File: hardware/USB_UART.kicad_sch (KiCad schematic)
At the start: 15 parts, among them Q17 BC847BS-7-F, SW1 SW_SPDT, U14 CP2102N-QFN20

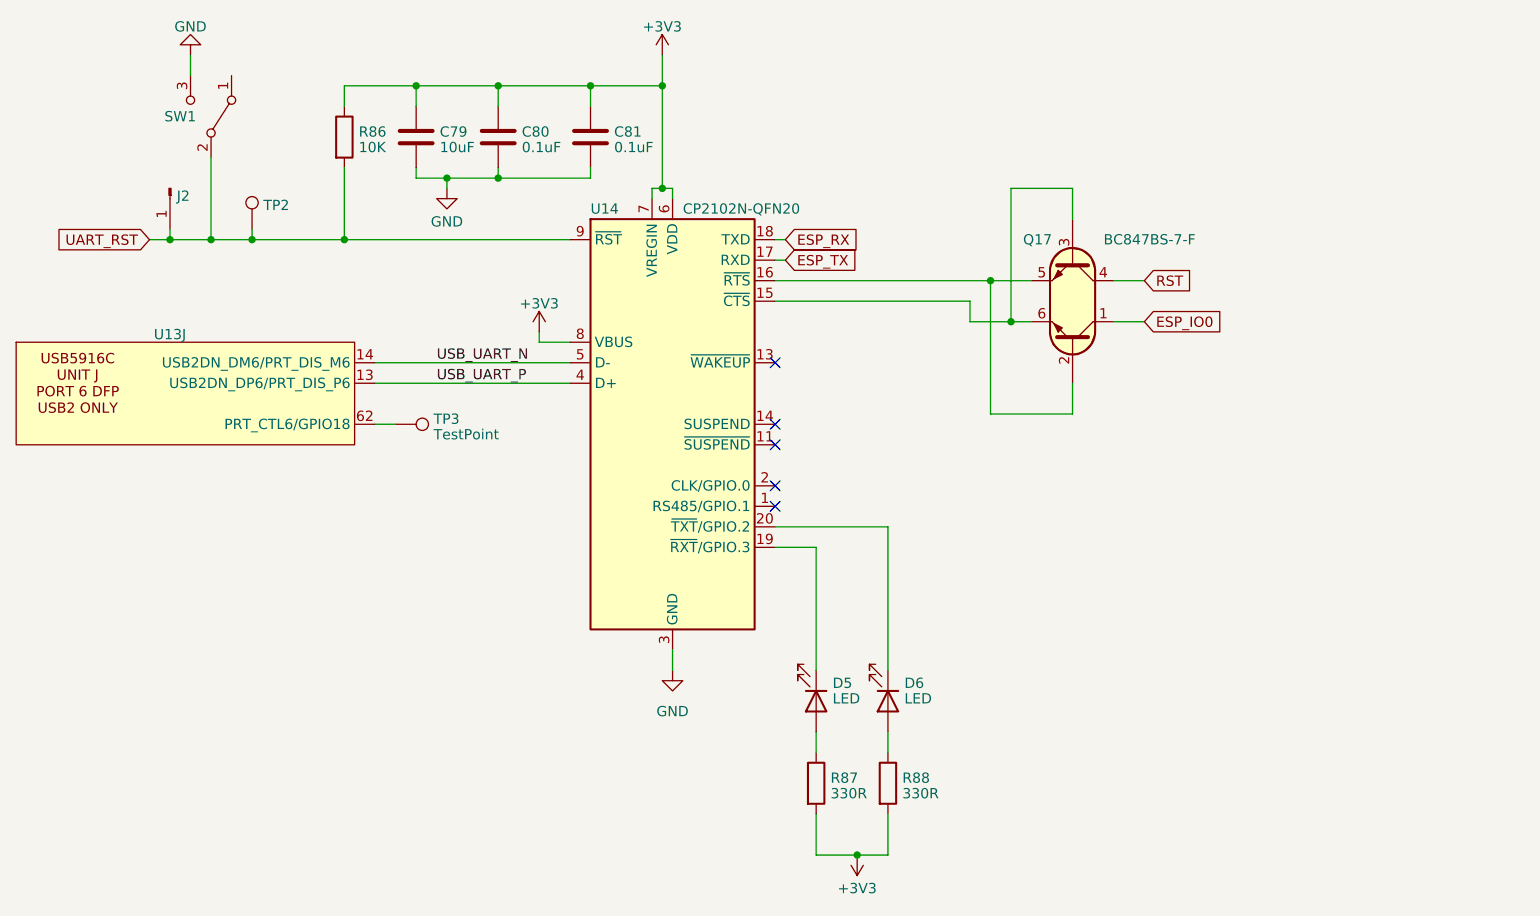
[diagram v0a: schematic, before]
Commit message: fixed DP issues and finneshed overall routeing
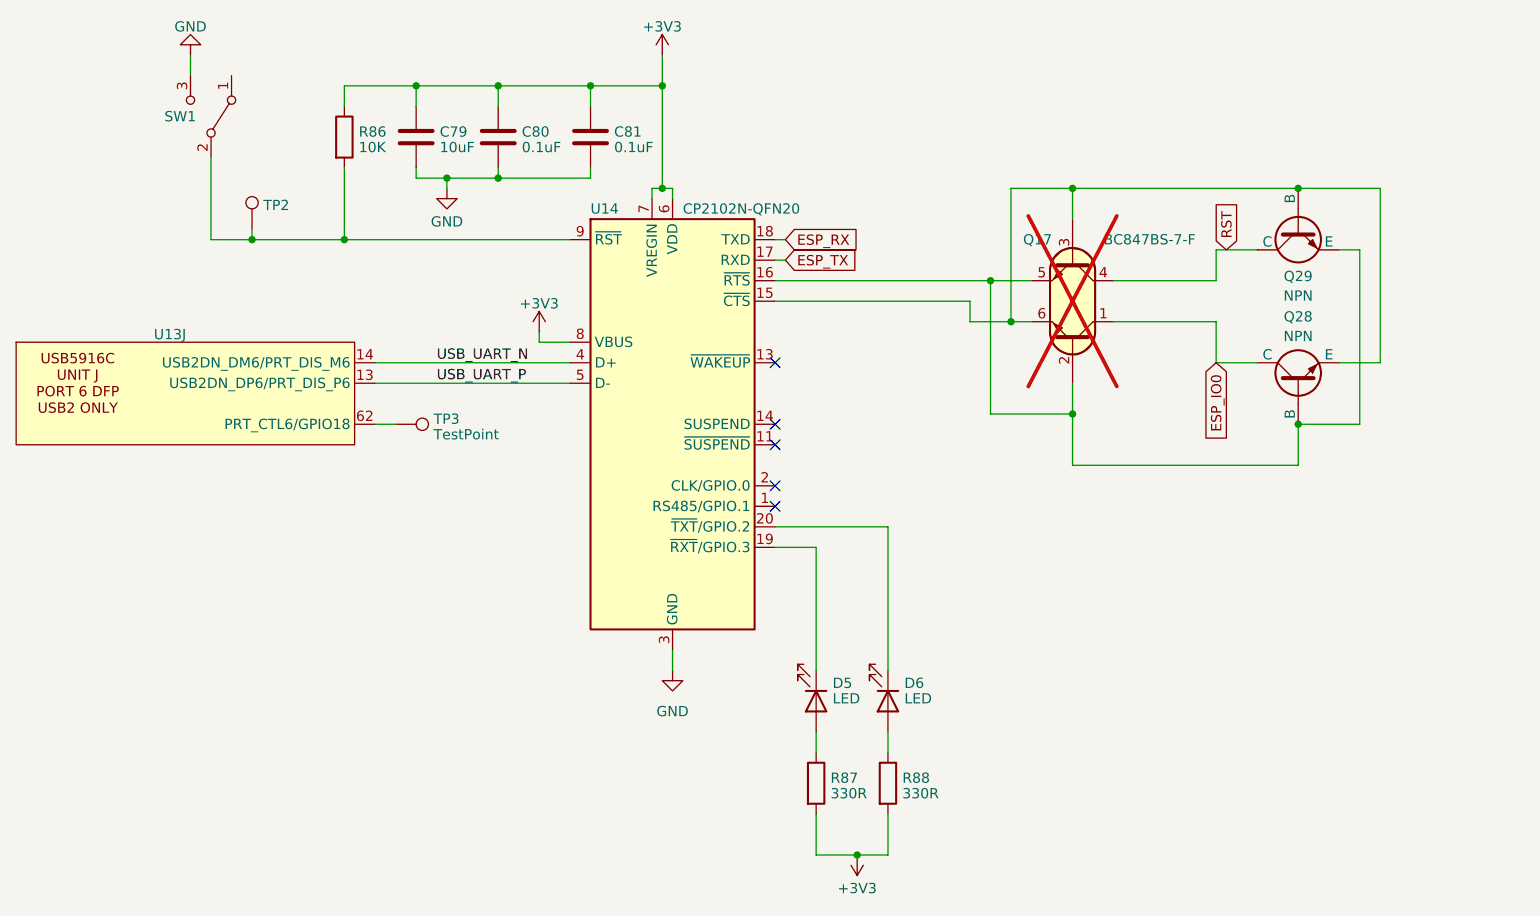
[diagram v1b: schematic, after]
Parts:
- removed J2: ~, Connector_PinHeader_2.54mm:PinHeader_1x01_P2.54mm_Vertical, symbol Connector:Conn_01x01_Pin
- added Q28, Q29: NPN, PCM_Package_TO_SOT_THT_AKL:TO-92L_ECB, symbol Simulation_SPICE:NPN
- Q17: now not fitted
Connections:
- net ESP_IO0: now also Q28.2 (C)
- net RST: now also Q29.2 (C)
- net USB_UART_N: now also U14.4 (D+); no longer U14.5 (D-)
- net USB_UART_P: now also U14.5 (D-); no longer U14.4 (D+)
- net at Q17.2 (B1), Q17.5 (E2), U14.16 (~{RTS}): now also Q28.3 (B), Q29.1 (E)
- net at Q17.3 (B2), Q17.6 (E1), U14.15 (~{CTS}): now also Q28.1 (E), Q29.3 (B)
- net UART_RST: no longer names the net of R86.2, SW1.2 (B), TP2.1, U14.9 (~{RST})
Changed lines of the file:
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@@
     (comment 3 "TOTAL SYSTEM POWER IS ~275w")
   )
+  (junction (at 181.61 57.15) (diameter 0) (color 0 0 0 0)
+  )
   (junction (at 110.49 44.45) (diameter 0) (color 0 0 0 0)
   )
@@
   (junction (at 130.81 57.15) (diameter 0) (color 0 0 0 0)
   )
-  (junction (at 74.93 63.5) (diameter 0) (color 0 0 0 0)
-  )
-  (junction (at 69.85 63.5) (diameter 0) (color 0 0 0 0)
-  )
   (junction (at 130.81 44.45) (diameter 0) (color 0 0 0 0)
+  )
+  (junction (at 209.55 86.36) (diameter 0) (color 0 0 0 0)
+  )
+  (junction (at 181.61 85.09) (diameter 0) (color 0 0 0 0)
+  )
+  (junction (at 209.55 57.15) (diameter 0) (color 0 0 0 0)
   )
   (junction (at 80.01 63.5) (diameter 0) (color 0 0 0 0)
@@
     (stroke (width 0) (type default))
   )
+  (wire (pts (xy 219.71 78.74) (xy 214.63 78.74))
+    (stroke (width 0) (type default))
+  )
   (wire (pts (xy 110.49 44.45) (xy 121.92 44.45))
     (stroke (width 0) (type default))
@@
     (stroke (width 0) (type default))
   )
+  (wire (pts (xy 219.71 57.15) (xy 219.71 78.74))
+    (stroke (width 0) (type default))
+  )
+  (wire (pts (xy 217.17 86.36) (xy 217.17 64.77))
+    (stroke (width 0) (type default))
+  )
   (wire (pts (xy 110.49 55.88) (xy 121.92 55.88))
     (stroke (width 0) (type default))
   )
-  (wire (pts (xy 186.69 68.58) (xy 190.5 68.58))
+  (wire (pts (xy 186.69 68.58) (xy 199.39 68.58))
+    (stroke (width 0) (type default))
+  )
+  (wire (pts (xy 181.61 57.15) (xy 209.55 57.15))
     (stroke (width 0) (type default))
   )
@@
     (stroke (width 0) (type default))
   )
+  (wire (pts (xy 199.39 68.58) (xy 199.39 64.77))
+    (stroke (width 0) (type default))
+  )
   (wire (pts (xy 80.01 62.23) (xy 80.01 63.5))
     (stroke (width 0) (type default))
@@
     (stroke (width 0) (type default))
   )
+  (wire (pts (xy 199.39 64.77) (xy 204.47 64.77))
+    (stroke (width 0) (type default))
+  )
+  (wire (pts (xy 209.55 86.36) (xy 217.17 86.36))
+    (stroke (width 0) (type default))
+  )
   (wire (pts (xy 154.94 139.7) (xy 158.75 139.7))
     (stroke (width 0) (type default))
   )
+  (wire (pts (xy 209.55 91.44) (xy 181.61 91.44))
+    (stroke (width 0) (type default))
+  )
   (wire (pts (xy 121.92 44.45) (xy 130.81 44.45))
     (stroke (width 0) (type default))
   )
-  (wire (pts (xy 186.69 73.66) (xy 190.5 73.66))
+  (wire (pts (xy 186.69 73.66) (xy 199.39 73.66))
     (stroke (width 0) (type default))
   )
@@
     (stroke (width 0) (type default))
   )
+  (wire (pts (xy 181.61 91.44) (xy 181.61 85.09))
+    (stroke (width 0) (type default))
+  )
   (wire (pts (xy 129.54 57.15) (xy 130.81 57.15))
     (stroke (width 0) (type default))
   )
-  (wire (pts (xy 69.85 63.5) (xy 74.93 63.5))
+  (wire (pts (xy 199.39 78.74) (xy 204.47 78.74))
+    (stroke (width 0) (type default))
+  )
+  (wire (pts (xy 199.39 73.66) (xy 199.39 78.74))
     (stroke (width 0) (type default))
   )
@@
     (stroke (width 0) (type default))
   )
-  (wire (pts (xy 67.31 63.5) (xy 69.85 63.5))
-    (stroke (width 0) (type default))
-  )
   (wire (pts (xy 100.33 55.88) (xy 104.14 55.88))
     (stroke (width 0) (type default))
@@
     (stroke (width 0) (type default))
   )
-  (wire (pts (xy 69.85 62.23) (xy 69.85 63.5))
-    (stroke (width 0) (type default))
-  )
   (wire (pts (xy 144.78 71.12) (xy 168.91 71.12))
     (stroke (width 0) (type default))
@@
     (stroke (width 0) (type default))
   )
+  (wire (pts (xy 209.55 86.36) (xy 209.55 91.44))
+    (stroke (width 0) (type default))
+  )
   (wire (pts (xy 121.92 44.45) (xy 121.92 46.99))
     (stroke (width 0) (type default))
   )
+  (wire (pts (xy 217.17 64.77) (xy 214.63 64.77))
+    (stroke (width 0) (type default))
+  )
   (wire (pts (xy 119.38 81.28) (xy 95.25 81.28))
     (stroke (width 0) (type default))
@@
   )
   (wire (pts (xy 168.91 71.12) (xy 168.91 73.66))
+    (stroke (width 0) (type default))
+  )
+  (wire (pts (xy 209.55 57.15) (xy 219.71 57.15))
     (stroke (width 0) (type default))
   )
@@
     )
   )
-  (global_label "RST" (shape input) (at 190.5 68.58 0) (fields_autoplaced)
+  (global_label "RST" (shape input) (at 200.66 64.77 90) (fields_autoplaced)
     (effects (font (size 1.27 1.27)) (justify left))
-    (property "Intersheetrefs" "${INTERSHEET_REFS}" (at 196.8529 68.58 0)
+    (property "Intersheetrefs" "${INTERSHEET_REFS}" (at 200.66 58.3377 90)
       (effects (font (size 1.27 1.27)) (justify left) hide)
     )
@@
     )
   )
-  (global_label "UART_RST" (shape input) (at 67.31 63.5 180) (fields_autoplaced)
+  (global_label "ESP_IO0" (shape input) (at 199.39 78.74 270) (fields_autoplaced)
     (effects (font (size 1.27 1.27)) (justify right))
-    (property "Intersheetrefs" "${INTERSHEET_REFS}" (at 55.3328 63.5 0)
+    (property "Intersheetrefs" "${INTERSHEET_REFS}" (at 199.39 89.4661 90)
       (effects (font (size 1.27 1.27)) (justify right) hide)
     )
   )
-  (global_label "ESP_IO0" (shape input) (at 190.5 73.66 0) (fields_autoplaced)
-    (effects (font (size 1.27 1.27)) (justify left))
-    (property "Intersheetrefs" "${INTERSHEET_REFS}" (at 201.1467 73.66 0)
-      (effects (font (size 1.27 1.27)) (justify left) hide)
-    )
-  )
   (symbol (lib_id "PCM_Transistor_BJT_AKL:Q_NPN_DUAL_Generic_C1B1B2C2E2E1") (at 181.61 71.12 270) (mirror x) (unit 1)
-    (in_bom yes) (on_board yes) (dnp no)
+    (in_bom yes) (on_board yes) (dnp yes)
     (property "Reference" "Q17" (at 179.07 63.5 90)
       (effects (font (size 1.27 1.27)) (justify right))
@@
           (reference "U13") (unit 10)
         )
-        (path "/fae025e9-99c5-40c1-af6f-99dc1edbfa43/7a7a6512-c96f-448a-bb8d-4d6e185adf7f"
-          (reference "U13") (unit 10)
-        )
       )
     )
@@
     )
   )
+  (symbol (lib_id "Simulation_SPICE:NPN") (at 209.55 81.28 90) (unit 1)
+    (in_bom yes) (on_board yes) (dnp no) (fields_autoplaced)
+    (property "Reference" "Q28" (at 209.55 73.0463 90)
+      (effects (font (size 1.27 1.27)))
+    )
+    (property "Value" "NPN" (at 209.55 75.4705 90)
+      (effects (font (size 1.27 1.27)))
+    )
+    (property "Footprint" "PCM_Package_TO_SOT_THT_AKL:TO-92L_ECB" (at 209.55 17.78 0)
+      (effects (font (size 1.27 1.27)) hide)
+    )
+    (property "Datasheet" "~" (at 209.55 17.78 0)
+      (effects (font (size 1.27 1.27)) hide)
+    )
+    (property "Sim.Device" "NPN" (at 209.55 81.28 0)
+      (effects (font (size 1.27 1.27)) hide)
+    )
+    (property "Sim.Type" "GUMMELPOON" (at 209.55 81.28 0)
+      (effects (font (size 1.27 1.27)) hide)
+    )
+    (property "Sim.Pins" "1=C 2=B 3=E" (at 209.55 81.28 0)
+      (effects (font (size 1.27 1.27)) hide)
+    )
+    (pin "3")
+    (pin "2")
+    (pin "1")
+    (instances
+      (project "usbc-car-module"
+        (path "/fae025e9-99c5-40c1-af6f-99dc1edbfa43/115036d9-3633-4f5d-a259-54a6f0cf58ce"
+          (reference "Q28") (unit 1)
+        )
+      )
+    )
+  )
   (symbol (lib_id "Device:R") (at 149.86 130.81 0) (unit 1)
     (in_bom yes) (on_board yes) (dnp no) (fields_autoplaced)
@@
         (path "/fae025e9-99c5-40c1-af6f-99dc1edbfa43/115036d9-3633-4f5d-a259-54a6f0cf58ce"
           (reference "D6") (unit 1)
-        )
-      )
-    )
-  )
-  (symbol (lib_id "Connector:Conn_01x01_Pin") (at 69.85 57.15 270) (unit 1)
-    (in_bom yes) (on_board yes) (dnp no) (fields_autoplaced)
-    (property "Reference" "J2" (at 70.6882 58.1018 90)
-      (effects (font (size 1.27 1.27)) (justify left))
-    )
-    (property "Value" "~" (at 70.6882 59.0623 90)
-      (effects (font (size 1.27 1.27)) (justify left))
-    )
-    (property "Footprint" "Connector_PinHeader_2.54mm:PinHeader_1x01_P2.54mm_Vertical" (at 69.85 57.15 0)
-      (effects (font (size 1.27 1.27)) hide)
-    )
-    (property "Datasheet" "~" (at 69.85 57.15 0)
-      (effects (font (size 1.27 1.27)) hide)
-    )
-    (pin "1")
-    (instances
-      (project "usbc-car-module"
-        (path "/fae025e9-99c5-40c1-af6f-99dc1edbfa43/115036d9-3633-4f5d-a259-54a6f0cf58ce"
-          (reference "J2") (unit 1)
         )
       )
@@
         )
       )
+    )
+  )
+  (symbol (lib_name "NPN_1") (lib_id "Simulation_SPICE:NPN") (at 209.55 62.23 90) (mirror x) (unit 1)
+    (in_bom yes) (on_board yes) (dnp no)
+    (property "Reference" "Q29" (at 209.55 68.0395 90)
+      (effects (font (size 1.27 1.27)))
+    )
+    (property "Value" "NPN" (at 209.55 70.4637 90)
+      (effects (font (size 1.27 1.27)))
+    )
+    (property "Footprint" "PCM_Package_TO_SOT_THT_AKL:TO-92L_ECB" (at 209.55 125.73 0)
+      (effects (font (size 1.27 1.27)) hide)
+    )
+    (property "Datasheet" "~" (at 209.55 125.73 0)
+      (effects (font (size 1.27 1.27)) hide)
+    )
+    (property "Sim.Device" "NPN" (at 209.55 62.23 0)
+      (effects (font (size 1.27 1.27)) hide)
+    )
+    (property "Sim.Type" "GUMMELPOON" (at 209.55 62.23 0)
+      (effects (font (size 1.27 1.27)) hide)
+    )
+    (property "Sim.Pins" "1=C 2=B 3=E" (at 209.55 62.23 0)
+      (effects (font (size 1.27 1.27)) hide)
+    )
+    (pin "3")
+    (pin "2")
+    (pin "1")
+    (instances
+      (project "usbc-car-module"
+        (path "/fae025e9-99c5-40c1-af6f-99dc1edbfa43/115036d9-3633-4f5d-a259-54a6f0cf58ce"
+          (reference "Q29") (unit 1)
+        )
+      )

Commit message: minor revisions
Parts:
- TP2: value ~ -> TestPoint
- U13: value ~ -> USB5926C
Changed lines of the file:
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@@
   )
   (symbol (lib_id "CARTHING:USB5916C") (at 71.12 87.63 0) (unit 10)
-    (in_bom yes) (on_board yes) (dnp no) (fields_autoplaced)
+    (in_bom yes) (on_board yes) (dnp no)
     (property "Reference" "U13" (at 69.85 75.2381 0)
       (effects (font (size 1.27 1.27)))
     )
-    (property "Value" "~" (at 63.5 55.88 0)
+    (property "Value" "USB5926C" (at 87.63 74.93 0)
       (effects (font (size 1.27 1.27)))
     )
@@
       (effects (font (size 1.27 1.27)) (justify left))
     )
-    (property "Value" "~" (at 81.407 60.2053 0)
-      (effects (font (size 1.27 1.27)) (justify left))
-    )
+    (property "Value" "TestPoint" (at 81.407 60.2053 0)
+      (effects (font (size 1.27 1.27)) (justify left))
+    )

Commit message: working on usb pd protocol implimentation
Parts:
- added JP12, JP14: ~, Jumper:SolderJumper-2_P1.3mm_Open_RoundedPad1.0x1.5mm, symbol Jumper:SolderJumper_2_Open
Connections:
- net ESP_RX: now also JP12.1 (A); no longer U14.18 (TXD)
- net ESP_TX: now also JP14.1 (A); no longer U14.17 (RXD)
- new net: JP14.2 (B), U14.17 (RXD)
- new net: JP12.2 (B), U14.18 (TXD)
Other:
- moved on the sheet: Q17, Q28, Q29

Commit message: kicad version upgrade and minor pcb changes
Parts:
- added TP1, TP34, TP35, TP36, TP37: TestPoint, TestPoint:TestPoint_Pad_D1.0mm, symbol Connector:TestPoint
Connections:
- net at U14.1 (RS485/GPIO.1): now also TP37.1
- net at U14.11 (~{SUSPEND}): now also TP35.1
- net at U14.13 (~{WAKEUP}): now also TP1.1
- net at U14.14 (SUSPEND): now also TP34.1
- net at U14.2 (CLK/GPIO.0): now also TP36.1
- no-connect marks 5 -> 0
